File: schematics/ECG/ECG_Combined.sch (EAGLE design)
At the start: 71 parts, among them IC1 ADS1293, IC2 LIS3DH, IC3 MCP1703, IC4 CC2541, IC5 FSA4157, IC6 FSA4157, IC7 FSA4157, IC8 BALUN_2450BM_SERIES_SMD, X1 XTAL-2SMD, X2 XTAL_403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

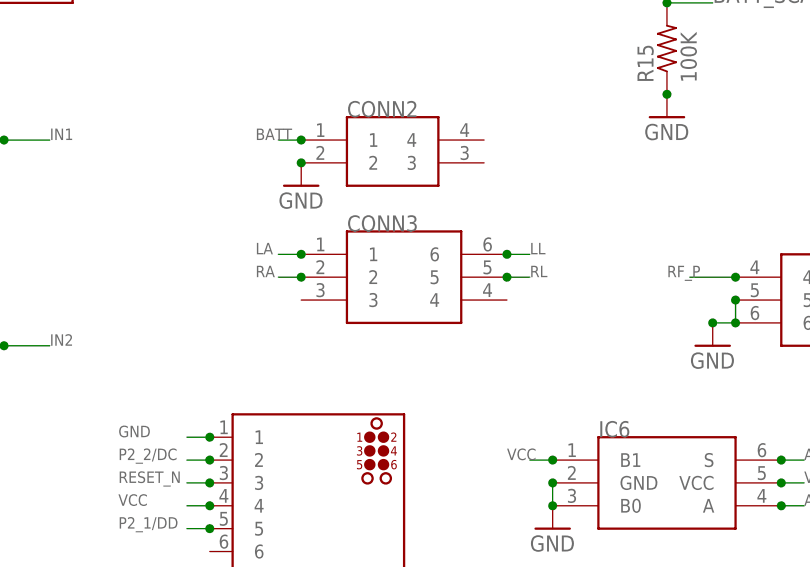
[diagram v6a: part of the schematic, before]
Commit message: adjusted board size. changed eeg pins
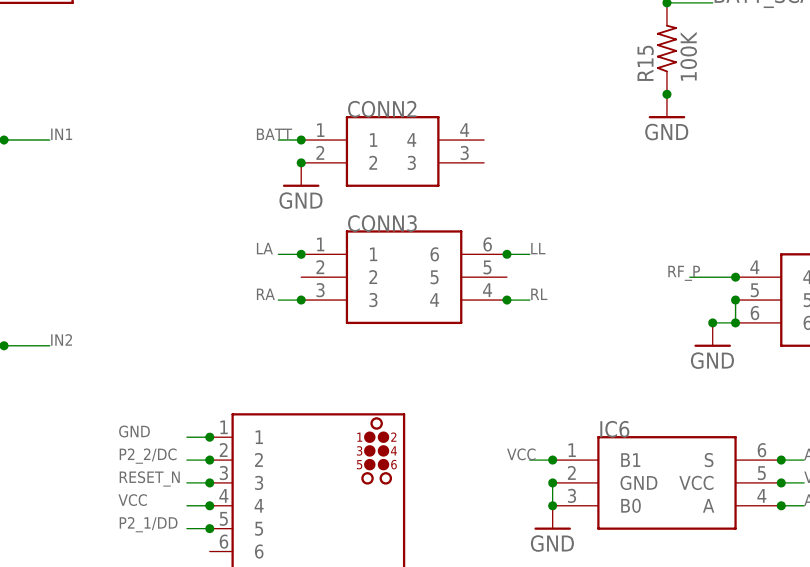
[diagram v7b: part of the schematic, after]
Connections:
- net RA: now also CONN3.3; no longer CONN3.2
- net RL: now also CONN3.4; no longer CONN3.5
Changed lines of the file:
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@@
 <grid distance="0.1" unitdist="inch" unit="inch" style="lines" multiple="1" display="no" altdistance="0.01" altunitdist="inch" altunit="inch"/>
 <layers>
-<layer number="1" name="Top" color="4" fill="1" visible="yes" active="no"/>
-<layer number="2" name="Route2" color="1" fill="3" visible="yes" active="no"/>
-<layer number="3" name="Route3" color="4" fill="3" visible="yes" active="no"/>
-<layer number="4" name="Route4" color="1" fill="4" visible="yes" active="no"/>
-<layer number="5" name="Route5" color="4" fill="4" visible="yes" active="no"/>
-<layer number="6" name="Route6" color="1" fill="8" visible="yes" active="no"/>
-<layer number="7" name="Route7" color="4" fill="8" visible="yes" active="no"/>
-<layer number="8" name="Route8" color="1" fill="2" visible="yes" active="no"/>
-<layer number="9" name="Route9" color="4" fill="2" visible="yes" active="no"/>
-<layer number="10" name="Route10" color="1" fill="7" visible="yes" active="no"/>
-<layer number="11" name="Route11" color="4" fill="7" visible="yes" active="no"/>
-<layer number="12" name="Route12" color="1" fill="5" visible="yes" active="no"/>
-<layer number="13" name="Route13" color="4" fill="5" visible="yes" active="no"/>
-<layer number="14" name="Route14" color="1" fill="6" visible="yes" active="no"/>
-<layer number="15" name="Route15" color="4" fill="6" visible="yes" active="no"/>
-<layer number="16" name="Bottom" color="1" fill="1" visible="yes" active="no"/>
-<layer number="17" name="Pads" color="2" fill="1" visible="yes" active="no"/>
-<layer number="18" name="Vias" color="2" fill="1" visible="yes" active="no"/>
-<layer number="19" name="Unrouted" color="6" fill="1" visible="yes" active="no"/>
-<layer number="20" name="Dimension" color="15" fill="1" visible="yes" active="no"/>
-<layer number="21" name="tPlace" color="7" fill="1" visible="yes" active="no"/>
-<layer number="22" name="bPlace" color="7" fill="1" visible="yes" active="no"/>
-<layer number="23" name="tOrigins" color="15" fill="1" visible="yes" active="no"/>
-<layer number="24" name="bOrigins" color="15" fill="1" visible="yes" active="no"/>
-<layer number="25" name="tNames" color="7" fill="1" visible="yes" active="no"/>
-<layer number="26" name="bNames" color="7" fill="1" visible="yes" active="no"/>
-<layer number="27" name="tValues" color="7" fill="1" visible="yes" active="no"/>
-<layer number="28" name="bValues" color="7" fill="1" visible="yes" active="no"/>
+<layer number="1" name="Top" color="4" fill="1" visible="no" active="no"/>
+<layer number="2" name="Route2" color="1" fill="3" visible="no" active="no"/>
+<layer number="3" name="Route3" color="4" fill="3" visible="no" active="no"/>
+<layer number="4" name="Route4" color="1" fill="4" visible="no" active="no"/>
+<layer number="5" name="Route5" color="4" fill="4" visible="no" active="no"/>
+<layer number="6" name="Route6" color="1" fill="8" visible="no" active="no"/>
+<layer number="7" name="Route7" color="4" fill="8" visible="no" active="no"/>
+<layer number="8" name="Route8" color="1" fill="2" visible="no" active="no"/>
+<layer number="9" name="Route9" color="4" fill="2" visible="no" active="no"/>
+<layer number="10" name="Route10" color="1" fill="7" visible="no" active="no"/>
+<layer number="11" name="Route11" color="4" fill="7" visible="no" active="no"/>
+<layer number="12" name="Route12" color="1" fill="5" visible="no" active="no"/>
+<layer number="13" name="Route13" color="4" fill="5" visible="no" active="no"/>
+<layer number="14" name="Route14" color="1" fill="6" visible="no" active="no"/>
+<layer number="15" name="Route15" color="4" fill="6" visible="no" active="no"/>
+<layer number="16" name="Bottom" color="1" fill="1" visible="no" active="no"/>
+<layer number="17" name="Pads" color="2" fill="1" visible="no" active="no"/>
+<layer number="18" name="Vias" color="2" fill="1" visible="no" active="no"/>
+<layer number="19" name="Unrouted" color="6" fill="1" visible="no" active="no"/>
+<layer number="20" name="Dimension" color="15" fill="1" visible="no" active="no"/>
+<layer number="21" name="tPlace" color="7" fill="1" visible="no" active="no"/>
+<layer number="22" name="bPlace" color="7" fill="1" visible="no" active="no"/>
+<layer number="23" name="tOrigins" color="15" fill="1" visible="no" active="no"/>
+<layer number="24" name="bOrigins" color="15" fill="1" visible="no" active="no"/>
+<layer number="25" name="tNames" color="7" fill="1" visible="no" active="no"/>
+<layer number="26" name="bNames" color="7" fill="1" visible="no" active="no"/>
+<layer number="27" name="tValues" color="7" fill="1" visible="no" active="no"/>
+<layer number="28" name="bValues" color="7" fill="1" visible="no" active="no"/>
 <layer number="29" name="tStop" color="7" fill="3" visible="no" active="no"/>
 <layer number="30" name="bStop" color="7" fill="6" visible="no" active="no"/>
@@
 <layer number="35" name="tGlue" color="7" fill="4" visible="no" active="no"/>
 <layer number="36" name="bGlue" color="7" fill="5" visible="no" active="no"/>
-<layer number="37" name="tTest" color="7" fill="1" visible="yes" active="no"/>
-<layer number="38" name="bTest" color="7" fill="1" visible="yes" active="no"/>
+<layer number="37" name="tTest" color="7" fill="1" visible="no" active="no"/>
+<layer number="38" name="bTest" color="7" fill="1" visible="no" active="no"/>
 <layer number="39" name="tKeepout" color="4" fill="11" visible="no" active="no"/>
 <layer number="40" name="bKeepout" color="1" fill="11" visible="no" active="no"/>
@@
 <layer number="44" name="Drills" color="7" fill="1" visible="no" active="no"/>
 <layer number="45" name="Holes" color="7" fill="1" visible="no" active="no"/>
-<layer number="46" name="Milling" color="3" fill="1" visible="yes" active="no"/>
-<layer number="47" name="Measures" color="7" fill="1" visible="yes" active="no"/>
-<layer number="48" name="Document" color="7" fill="1" visible="yes" active="no"/>
-<layer number="49" name="Reference" color="7" fill="1" visible="yes" active="no"/>
-<layer number="50" name="dxf" color="7" fill="1" visible="yes" active="no"/>
-<layer number="51" name="tDocu" color="7" fill="1" visible="yes" active="no"/>
-<layer number="52" name="bDocu" color="7" fill="1" visible="yes" active="no"/>
-<layer number="53" name="tGND_GNDA" color="7" fill="9" visible="yes" active="no"/>
-<layer number="54" name="bGND_GNDA" color="1" fill="9" visible="yes" active="no"/>
-<layer number="56" name="wert" color="7" fill="1" visible="yes" active="no"/>
+<layer number="46" name="Milling" color="3" fill="1" visible="no" active="no"/>
+<layer number="47" name="Measures" color="7" fill="1" visible="no" active="no"/>
+<layer number="48" name="Document" color="7" fill="1" visible="no" active="no"/>
+<layer number="49" name="Reference" color="7" fill="1" visible="no" active="no"/>
+<layer number="50" name="dxf" color="7" fill="1" visible="no" active="no"/>
+<layer number="51" name="tDocu" color="7" fill="1" visible="no" active="no"/>
+<layer number="52" name="bDocu" color="7" fill="1" visible="no" active="no"/>
+<layer number="53" name="tGND_GNDA" color="7" fill="9" visible="no" active="no"/>
+<layer number="54" name="bGND_GNDA" color="1" fill="9" visible="no" active="no"/>
+<layer number="56" name="wert" color="7" fill="1" visible="no" active="no"/>
 <layer number="91" name="Nets" color="2" fill="1" visible="yes" active="yes"/>
 <layer number="92" name="Busses" color="1" fill="1" visible="yes" active="yes"/>
@@
 </segment>
 <segment>
-<pinref part="CONN3" gate="CONN" pin="2"/>
-<wire x1="60.96" y1="160.02" x2="58.42" y2="160.02" width="0.1524" layer="91"/>
-<junction x="60.96" y="160.02"/>
-<label x="55.88" y="160.02" size="1.27" layer="95"/>
+<pinref part="CONN3" gate="CONN" pin="3"/>
+<wire x1="60.96" y1="157.48" x2="58.42" y2="157.48" width="0.1524" layer="91"/>
+<junction x="60.96" y="157.48"/>
+<label x="55.88" y="157.48" size="1.27" layer="95"/>
 </segment>
 </net>
@@
 </segment>
 <segment>
-<pinref part="CONN3" gate="CONN" pin="5"/>
-<wire x1="83.82" y1="160.02" x2="86.36" y2="160.02" width="0.1524" layer="91"/>
-<junction x="83.82" y="160.02"/>
-<label x="86.36" y="160.02" size="1.27" layer="95"/>
+<pinref part="CONN3" gate="CONN" pin="4"/>
+<wire x1="83.82" y1="157.48" x2="86.36" y2="157.48" width="0.1524" layer="91"/>
+<junction x="83.82" y="157.48"/>
+<label x="86.36" y="157.48" size="1.27" layer="95"/>
 </segment>
 </net>

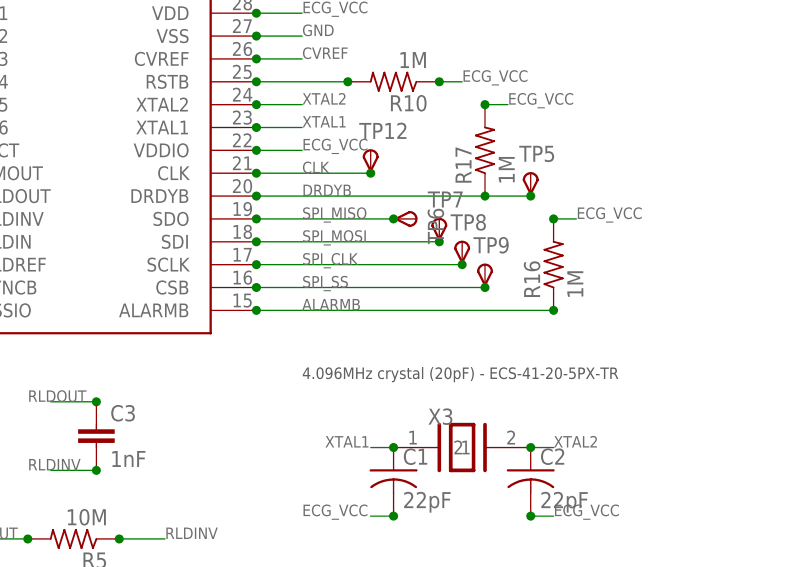
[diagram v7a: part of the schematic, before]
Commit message: added TP to ALARMB pin
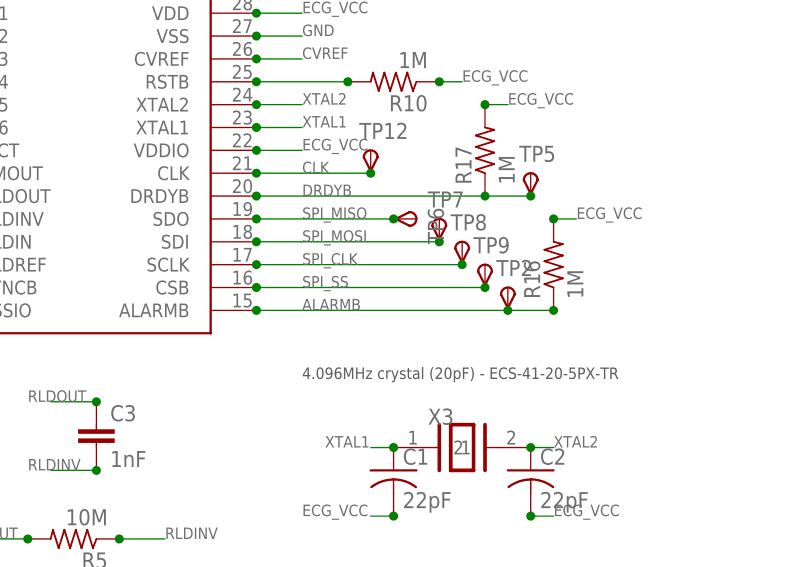
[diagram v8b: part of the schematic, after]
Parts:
- added TP2: TPSTP06R, testpad:TPSTP06R
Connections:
- net ALARMB: now also TP2.PP
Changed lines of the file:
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@@
 <part name="U$5" library="tagconnect" deviceset="TC2030" device="-MCP-NL"/>
 <part name="TP1" library="testpad" deviceset="TPS" device="TP08SQ"/>
+<part name="TP2" library="testpad" deviceset="TPS" device="TP06R" value="TPSTP06R"/>
 </parts>
 <sheets>
@@
 <instance part="U$5" gate="G$1" x="63.5" y="134.62"/>
 <instance part="TP1" gate="G$1" x="96.52" y="119.38"/>
+<instance part="TP2" gate="G$1" x="119.38" y="43.18"/>
 </instances>
 <busses>
@@
 <pinref part="IC1" gate="IC" pin="ALARMB"/>
 <junction x="91.44" y="40.64"/>
-<wire x1="91.44" y1="40.64" x2="124.46" y2="40.64" width="0.1524" layer="91"/>
+<wire x1="91.44" y1="40.64" x2="119.38" y2="40.64" width="0.1524" layer="91"/>
 <label x="96.52" y="40.64" size="1.27" layer="95"/>
 <pinref part="R16" gate="G$1" pin="1"/>
 <junction x="124.46" y="40.64"/>
-</segment>
-<segment>
+<pinref part="TP2" gate="G$1" pin="PP"/>
+<wire x1="119.38" y1="40.64" x2="124.46" y2="40.64" width="0.1524" layer="91"/>
+<junction x="119.38" y="40.64"/>
+</segment>
+<segment>
